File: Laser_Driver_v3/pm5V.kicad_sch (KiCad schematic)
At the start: 22 parts, among them U47 MC7808CTG, U48 LM7905_TO220, U49 LT3045EMSE 5V, U50 LT3094EMSE -5V, U51 OPA192IDR

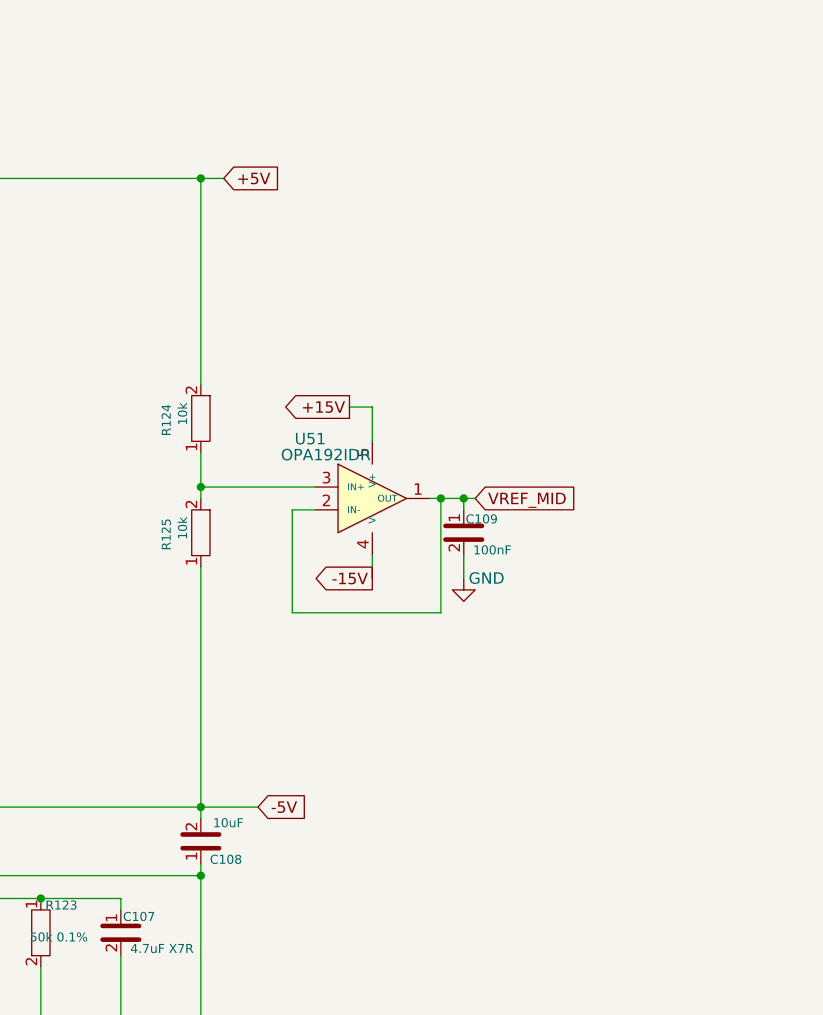
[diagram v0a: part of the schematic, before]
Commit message: Split into a power and signal board.
I think all footprints are now valid.  Need to figure out the power connections between boards, currently just screw terminals for wire.  I think a single multi-pin connector will work, but want to find something with premade off the shelf cables.
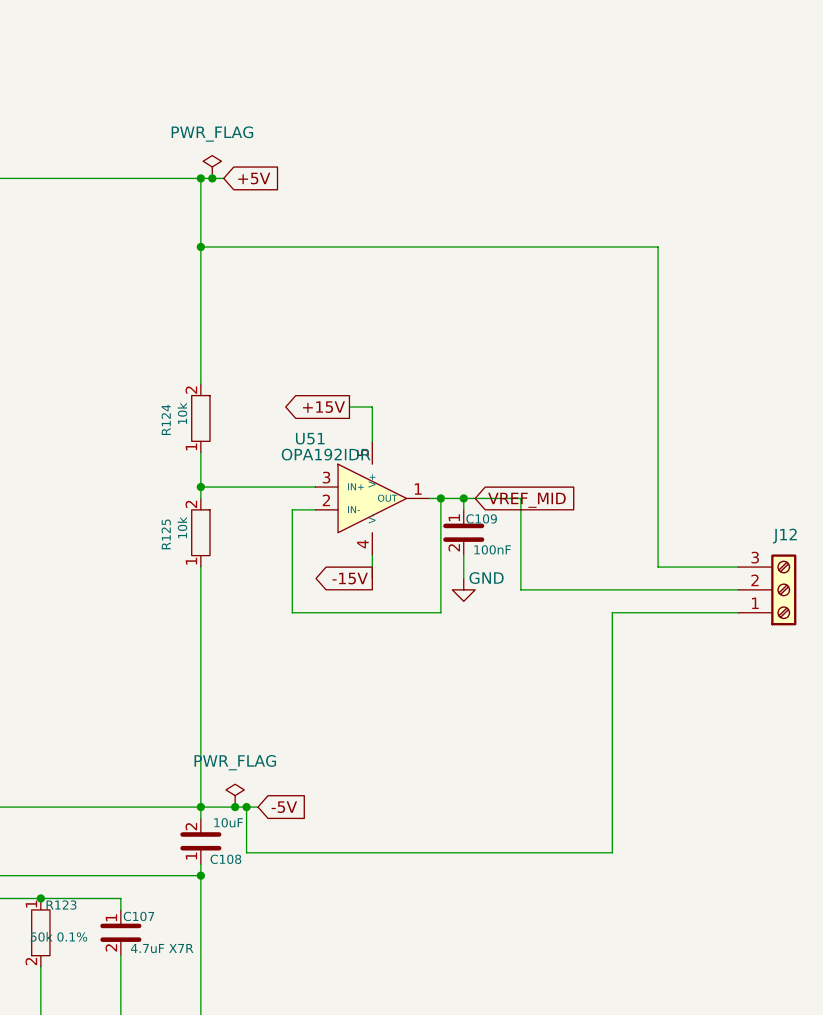
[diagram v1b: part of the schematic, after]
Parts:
- added J12: Screw_Terminal_01x03, Connector_Phoenix_MSTB:PhoenixContact_MSTBA_2,5_3-G-5,08_1x03_P5.08mm_Horizontal, symbol Connector:Screw_Terminal_01x03
- U49, U50: footprint Package_SO:Analog_MSOP-12-16-1EP_3x4.039mm_P0.5mm_EP1.651x2.845mm_ThermalVias -> Package_SO:MSOP-12-1EP_3x4.039mm_P0.65mm_EP1.651x2.845mm_ThermalVias
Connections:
- net +5V: now also J12.3 (Pin_3)
- net -5V: now also J12.1 (Pin_1)
- net VREF_MID: now also J12.2 (Pin_2)

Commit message: First power pcb layout without traces.
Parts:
- removed J12: Screw_Terminal_01x03, Connector_Phoenix_MSTB:PhoenixContact_MSTBA_2,5_3-G-5,08_1x03_P5.08mm_Horizontal, symbol Connector:Screw_Terminal_01x03
- added C110, C111: 100nF, Capacitor_SMD:C_0805_2012Metric_Pad1.18x1.45mm_HandSolder, symbol Device:C
- added D26: 1N4007, Diode_THT:D_DO-15_P12.70mm_Horizontal, symbol Diode:1N4007
- U50: footprint Package_SO:MSOP-12-1EP_3x4.039mm_P0.65mm_EP1.651x2.845mm_ThermalVias -> Package_SO:MSOP-12-1EP_3x4.039mm_P0.65mm_EP1.651x2.845mm; symbol Regulator_Linear:LT3042 -> Regulator_Linear:LT3094xMSE
- U51: footprint Package_SO:SOIC-8_3.9x4.9mm_P1.27mm -> Package_TO_SOT_SMD:SOT-23-5_HandSoldering
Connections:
- net +15V: now also C110.1
- net -15V: now also C111.1
- net -22V: now also D26.2 (A)
- net GND: now also C110.2, C111.2
- net at C103.2, C106.1, U48.3 (VO)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: now also U50.13 (IN), D26.1 (K)
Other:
- moved on the sheet: C106, C107, R122, R123

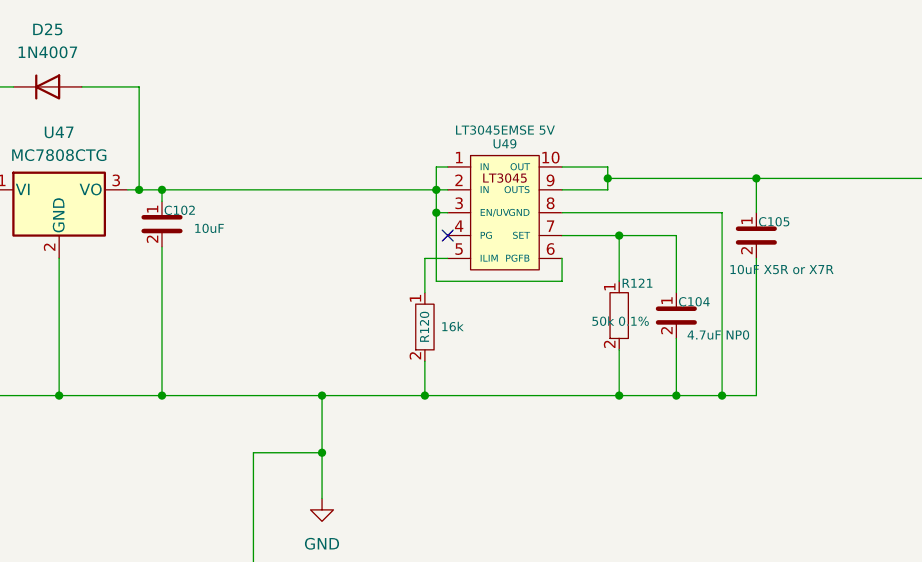
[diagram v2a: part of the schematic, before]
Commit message: Updated LT3045 footprints started Cu pours
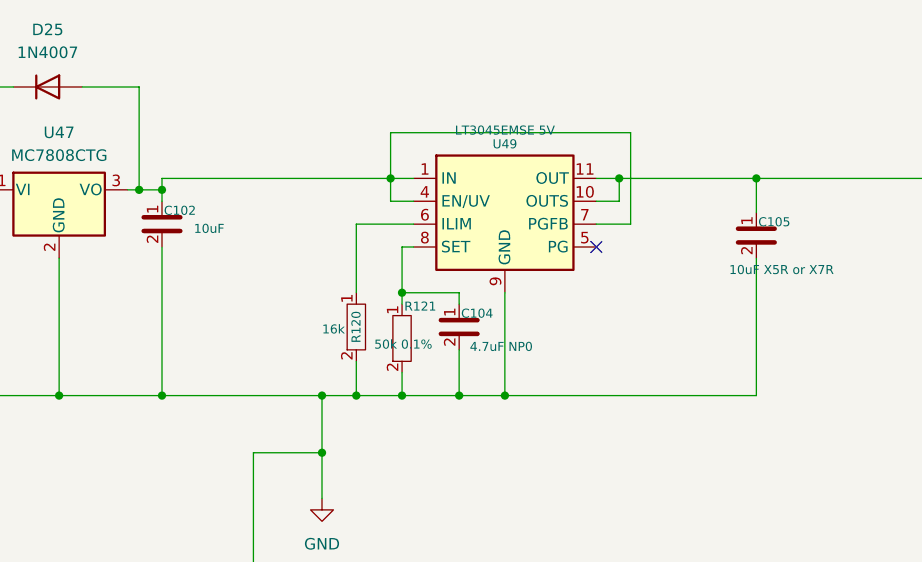
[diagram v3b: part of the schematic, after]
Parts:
- U49: footprint Package_SO:MSOP-12-1EP_3x4.039mm_P0.65mm_EP1.651x2.845mm_ThermalVias -> Package_SO:MSOP-12-1EP_3x4.039mm_P0.65mm_EP1.651x2.845mm; symbol Regulator_Linear:LT3042 -> Regulator_Linear:LT3045xMSE
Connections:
- net +5V: now also U49.11 (OUT), U49.12 (OUT); no longer U49.9 (OUTS)
- net GND: now also U49.13 (GND), U49.9 (GND); no longer U49.8 (GND)
- net at R120.1: now also U49.6 (ILIM); no longer U49.5 (ILIM)
- net at C102.1, D25.2 (A), U47.3 (VO)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: now also U49.4 (EN/UV), U49.7 (PGFB); no longer U49.6 (PGFB)
- net at C104.1, R121.1: now also U49.8 (SET); no longer U49.7 (SET)
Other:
- moved on the sheet: C104, R120, R121

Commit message: updated to newer/available parts
Routing needs to be completely redone.
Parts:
- C67: renamed from C104; value 4.7uF NP0 -> 4.7uF X7R
- U21: renamed from U51; value OPA192IDR -> OPA192IDBVR
- renumbered C100 to C63, C101 to C64, C102 to C65, C103 to C66, C106 to C68, C105 to C69, C107 to C70, C108 to C71, C110 to C72, C111 to C73, C109 to C74, D25 to D14, D26 to D15, R120 to R44, R121 to R45, R123 to R46, R122 to R47, R124 to R48, R125 to R49, U47 to U17, U48 to U18, U49 to U19, U50 to U20

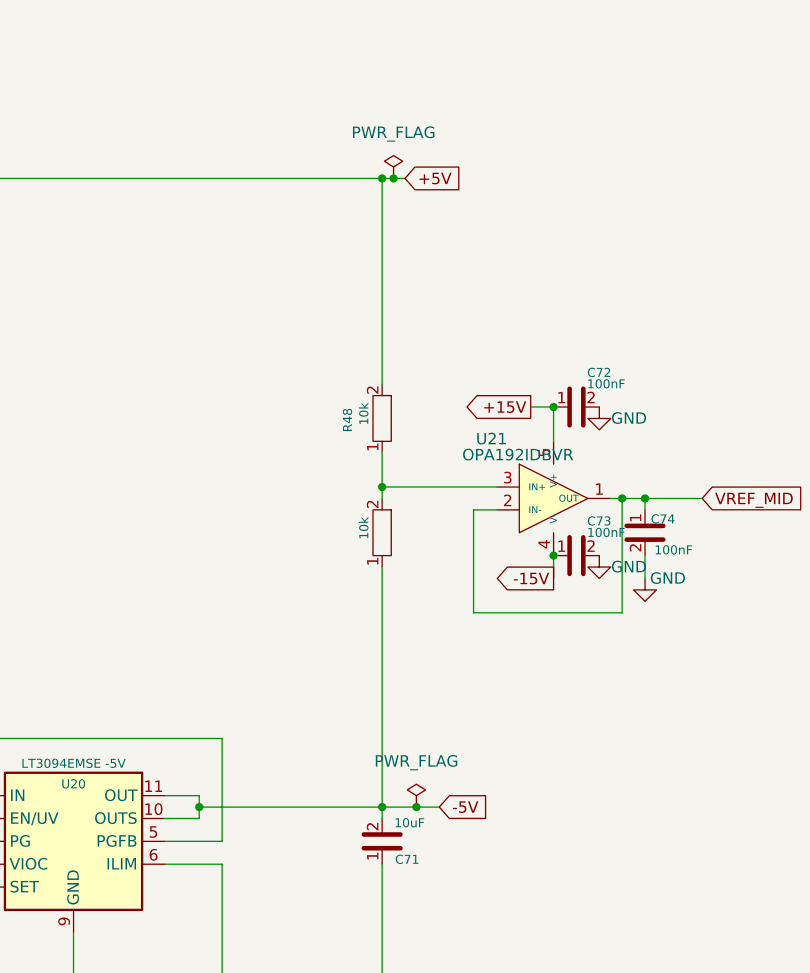
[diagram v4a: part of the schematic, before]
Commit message: Adding rail voltage good led circuitry.
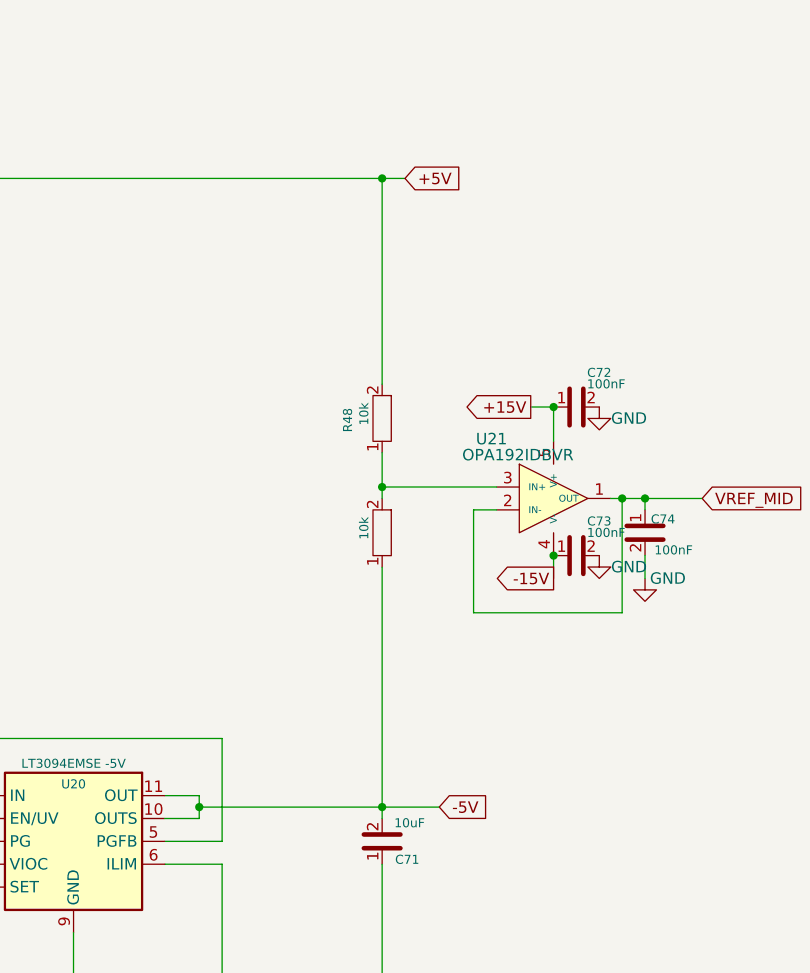
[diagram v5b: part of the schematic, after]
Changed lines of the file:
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@@
 	)
 	(junction
-		(at 199.39 114.3)
-		(diameter 0)
-		(color 0 0 0 0)
-	)
-	(junction
 		(at 175.26 114.3)
 		(diameter 0)
@@
 	)
 	(junction
-		(at 196.85 44.45)
-		(diameter 0)
-		(color 0 0 0 0)
-	)
-	(junction
 		(at 72.39 114.3)
 		(diameter 0)
@@
 	(wire
 		(pts
-			(xy 199.39 114.3) (xy 201.93 114.3)
+			(xy 195.58 114.3) (xy 201.93 114.3)
 		)
 		(stroke
@@
 	(wire
 		(pts
-			(xy 196.85 44.45) (xy 198.12 44.45)
+			(xy 195.58 44.45) (xy 198.12 44.45)
 		)
 		(stroke
@@
 	(wire
 		(pts
-			(xy 195.58 44.45) (xy 196.85 44.45)
-		)
-		(stroke
-			(width 0)
-			(type default)
-		)
-	)
-	(wire
-		(pts
 			(xy 195.58 114.3) (xy 195.58 115.57)
 		)
@@
 	(wire
 		(pts
-			(xy 195.58 114.3) (xy 199.39 114.3)
-		)
-		(stroke
-			(width 0)
-			(type default)
-		)
-	)
-	(wire
-		(pts
 			(xy 68.58 102.87) (xy 68.58 93.98)
 		)
@@
 	)
 	(symbol
-		(lib_id "power:PWR_FLAG")
-		(at 196.85 44.45 0)
-		(unit 1)
-		(body_style 1)
-		(exclude_from_sim no)
-		(in_bom yes)
-		(on_board yes)
-		(in_pos_files yes)
-		(dnp no)
-		(fields_autoplaced yes)
-		(property "Reference" "#FLG06"
-			(at 196.85 42.545 0)
-			(hide yes)
-			(show_name no)
-			(do_not_autoplace no)
-			(effects
-				(font
-					(size 1.27 1.27)
-				)
-			)
-		)
-		(property "Value" "PWR_FLAG"
-			(at 196.85 39.37 0)
-			(show_name no)
-			(do_not_autoplace no)
-			(effects
-				(font
-					(size 1.27 1.27)
-				)
-			)
-		)
-		(property "Footprint" ""
-			(at 196.85 44.45 0)
-			(hide yes)
-			(show_name no)
-			(do_not_autoplace no)
-			(effects
-				(font
-					(size 1.27 1.27)
-				)
-			)
-		)
-		(property "Datasheet" ""
-			(at 196.85 44.45 0)
-			(hide yes)
-			(show_name no)
-			(do_not_autoplace no)
-			(effects
-				(font
-					(size 1.27 1.27)
-				)
-			)
-		)
-		(property "Description" "Special symbol for telling ERC where power comes from"
-			(at 196.85 44.45 0)
-			(hide yes)
-			(show_name no)
-			(do_not_autoplace no)
-			(effects
-				(font
-					(size 1.27 1.27)
-				)
-			)
-		)
-		(pin "1"
-		)
-		(instances
-			(project "laser_driver_v3_Power"
-				(path "/b2c3d4e5-f6a7-8901-bcde-f12345678901/5e81dcd4-9b1b-47dc-9619-b54132a8671e"
-					(reference "#FLG06")
-					(unit 1)
-				)
-			)
-		)
-	)
-	(symbol
 		(lib_id "Device:C")
 		(at 195.58 118.11 180)
@@
 					(unit 1)
 				)
-			)
-		)
-	)
-	(symbol
-		(lib_id "power:PWR_FLAG")
-		(at 199.39 114.3 0)
-		(unit 1)
-		(body_style 1)
-		(exclude_from_sim no)
-		(in_bom yes)
-		(on_board yes)
-		(in_pos_files yes)
-		(dnp no)
-		(fields_autoplaced yes)
-		(property "Reference" "#FLG07"
-			(at 199.39 112.395 0)
-			(hide yes)
-			(show_name no)
-			(do_not_autoplace no)
-			(effects
-				(font
-					(size 1.27 1.27)
-				)
-			)
-		)
-		(property "Value" "PWR_FLAG"
-			(at 199.39 109.22 0)
-			(show_name no)
-			(do_not_autoplace no)
-			(effects
-				(font
-					(size 1.27 1.27)
-				)
-			)
-		)
-		(property "Footprint" ""
-			(at 199.39 114.3 0)
-			(hide yes)
-			(show_name no)
-			(do_not_autoplace no)
-			(effects
-				(font
-					(size 1.27 1.27)
-				)
-			)
-		)
-		(property "Datasheet" ""
-			(at 199.39 114.3 0)
-			(hide yes)
-			(show_name no)
-			(do_not_autoplace no)
-			(effects
-				(font
-					(size 1.27 1.27)
-				)
-			)
-		)
-		(property "Description" "Special symbol for telling ERC where power comes from"
-			(at 199.39 114.3 0)
-			(hide yes)
-			(show_name no)
-			(do_not_autoplace no)
-			(effects
-				(font
-					(size 1.27 1.27)
-				)
-			)
-		)
-		(pin "1"
-		)
-		(instances
-			(project "laser_driver_v3_Power"
-				(path "/b2c3d4e5-f6a7-8901-bcde-f12345678901/5e81dcd4-9b1b-47dc-9619-b54132a8671e"
-					(reference "#FLG07")
-					(unit 1)
-				)

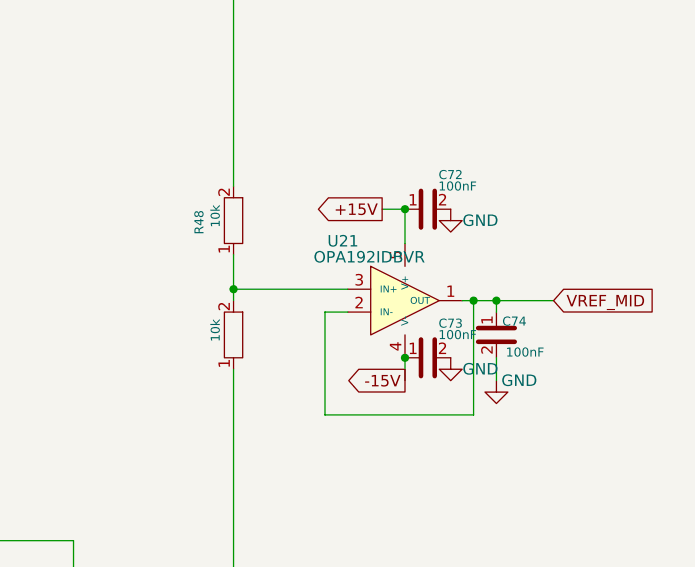
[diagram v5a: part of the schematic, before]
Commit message: Started placing voltage monitor parts.
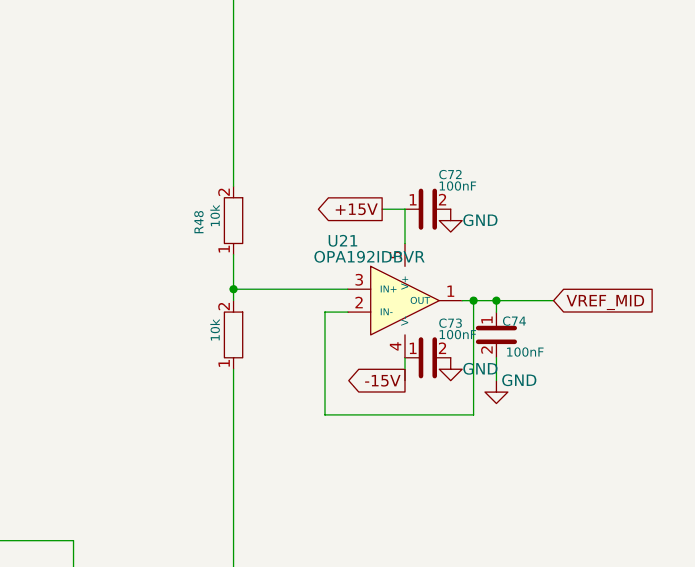
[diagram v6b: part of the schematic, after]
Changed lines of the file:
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@@
 	)
 	(junction
-		(at 214.63 69.85)
-		(diameter 0)
-		(color 0 0 0 0)
-	)
-	(junction
 		(at 132.08 114.3)
 		(diameter 0)
@@
 	)
 	(junction
-		(at 214.63 86.36)
-		(diameter 0)
-		(color 0 0 0 0)
-	)
-	(junction
 		(at 96.52 44.45)
 		(diameter 0)
@@
 	)
 	(symbol
+		(lib_name "C_1")
 		(lib_id "Device:C")
 		(at 68.58 105.41 0)
@@
 	)
 	(symbol
+		(lib_name "C_3")
 		(lib_id "Device:C")
 		(at 93.98 105.41 0)
@@
 	)
 	(symbol
+		(lib_name "C_4")
 		(lib_id "Device:C")
 		(at 137.16 50.8 0)
@@
 	)
 	(symbol
+		(lib_name "C_2")
 		(lib_id "Device:C")
 		(at 45.72 49.53 0)
@@
 	)
 	(symbol
+		(lib_name "C_9")
 		(lib_id "Device:C")
 		(at 224.79 83.82 0)
@@
 	)
 	(symbol
+		(lib_name "R_5")
 		(lib_id "Device:R")
 		(at 92.71 60.96 0)
@@
 	)
 	(symbol
+		(lib_name "R_4")
 		(lib_id "Device:R")
 		(at 195.58 83.82 180)
@@
 	)
 	(symbol
+		(lib_name "C_8")
 		(lib_id "Device:C")
 		(at 71.12 49.53 0)
@@
 	)
 	(symbol
+		(lib_name "C_7")
 		(lib_id "Device:C")
 		(at 132.08 123.19 0)
@@
 	)
 	(symbol
+		(lib_name "C_11")
 		(lib_id "Device:C")
 		(at 217.17 86.36 90)
@@
 	)
 	(symbol
+		(lib_name "C_10")
 		(lib_id "Device:C")
 		(at 146.05 133.35 0)
@@
 	)
 	(symbol
+		(lib_name "R_3")
 		(lib_id "Device:R")
 		(at 137.16 133.35 0)
@@
 	)
 	(symbol
+		(lib_name "C_6")
 		(lib_id "Device:C")
 		(at 104.14 60.96 0)
@@
 	)
 	(symbol
+		(lib_name "C_5")
 		(lib_id "Device:C")
 		(at 217.17 69.85 90)
@@
 	)
 	(symbol
+		(lib_name "R_2")
 		(lib_id "Device:R")
 		(at 177.8 138.43 0)
@@
 	)
 	(symbol
+		(lib_name "R_1")
 		(lib_id "Device:R")
 		(at 97.79 62.23 0)
